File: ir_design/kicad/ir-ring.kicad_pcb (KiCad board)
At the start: 2 copper layers, 40.3 x 43.1 mm, 24 parts, among them J1 PicoBlade/MX1.25 5p R/A THT, Q1 AO3400A, U1 SY7200A, U2 TEMT6200FX01

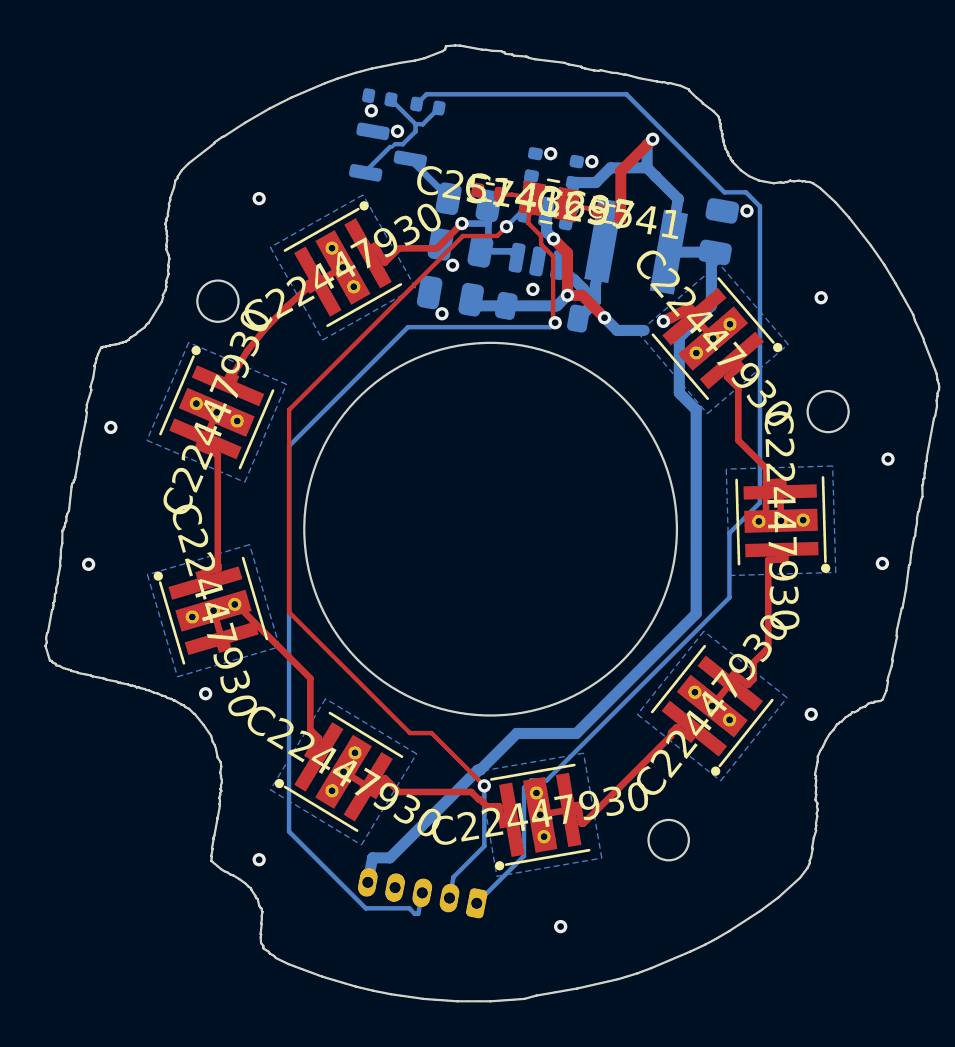
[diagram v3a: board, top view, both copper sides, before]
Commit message: feat(ir): spread the back side, 0805 passives, test pads
Only the switching loop stays packed in the top gap, now with >= 0.3 mm
courtyard gaps (was 0.03-0.1 mm, with L1/C1/C2 cutting into the thermal
islands). The DC-only half-power switch (Q1, R3, R4) moves to the D7-D8 gap;
09 asserts island, screw-head and courtyard clearances.

- all 0402 passives -> 0805; C2 -> 1206 X7R (C29823) for DC-bias margin
- TP1 VOUT (on D2's VOUT island), TP2 FB, TP3 GND, out of the BOM
- power stage pre-routed and closed on B.Cu; Freerouting re-solved it
  differently every run and stopped finding the VOUT crossing
- LCSC field hidden: it was printed on the silkscreen (78 -> 9 silk warnings)

DRC with --schematic-parity: 0 violations, 0 unconnected, 0 footprint errors.

Co-Authored-By: Claude Opus 5.5 <noreply@anthropic.com>
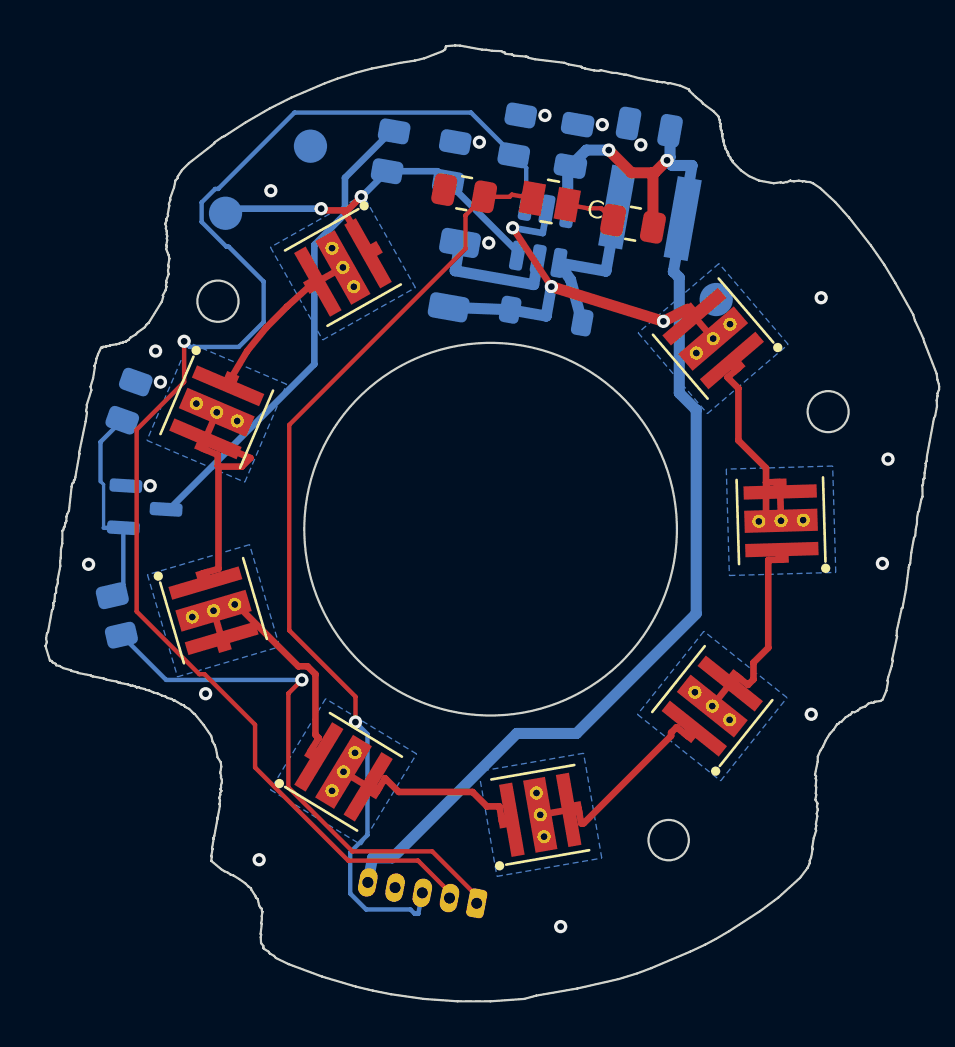
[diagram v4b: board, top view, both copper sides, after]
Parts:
- added TP1: VOUT, TestPoint:TestPoint_Pad_D1.5mm, B.Cu at (158.7, 94.6)
- added TP2: FB, TestPoint:TestPoint_Pad_D1.5mm, B.Cu at (136.5, 90.8)
- added TP3: GND, TestPoint:TestPoint_Pad_D1.5mm, B.Cu at (140.4, 87.7)
- C2: value 4.7uF 50V -> 4.7uF 50V X7R; footprint Capacitor_SMD:C_0805_2012Metric -> Capacitor_SMD:C_1206_3216Metric
- C3: footprint Capacitor_SMD:C_0402_1005Metric -> Capacitor_SMD:C_0805_2012Metric
- R2, R3, R4, R6, R7: footprint Resistor_SMD:R_0402_1005Metric -> Resistor_SMD:R_0805_2012Metric
- moved R3 26.9 mm to (131.6, 108.9), turned to 103 degrees
- moved Q1 19.3 mm to (132.9, 104.0), turned to -3.5 degrees
- moved R4 17.8 mm to (132.2, 99.2), turned to 70.5 degrees
- moved C1 5.66 mm to (155.7, 86.9), turned to 170 degrees
- moved R1b 4.20 mm to (144.0, 88.0), turned to 80 degrees
- moved R1a 3.89 mm to (146.7, 88.4), turned to 80 degrees
- moved L1 1.64 mm to (155.7, 90.7)
- moved R2 1.51 mm to (149.7, 87.2)
- moved C3 1.21 mm to (152.3, 87.7)
- moved R7 1.14 mm to (154.9, 91.2)
- moved R6 1.11 mm to (147.3, 89.8)
- moved C2 0.96 mm to (146.9, 93.5), turned to 80 degrees
- moved D1 0.24 mm to (151.0, 95.4)
- moved U1 0.10 mm to (150.8, 91.7)
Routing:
- net /WL_EN: track 54.9 -> 24.9 mm, vias 0 -> 1
- net /IL_EN: track 42.8 -> 63.7 mm, vias 2 -> 1
- net /R1B_Q: track 2.49 -> 21.5 mm
- net /FB: track 10.5 -> 18.4 mm, vias 1 -> 2
- net GND: track 0.00 -> 6.04 mm, vias 18 -> 17
- net /LDR: track 47.6 -> 43.5 mm
- net /VOUT: track 15.5 -> 19.2 mm, vias 4 -> 3
- net /Q1_G: track 6.32 -> 9.48 mm
- net /STR6: track 9.44 -> 12.3 mm
- net /SW: track 6.42 -> 8.01 mm
- net +5V: track 54.6 -> 53.6 mm, vias 1 -> 2
- net /U2_C: track 1.50 -> 2.30 mm

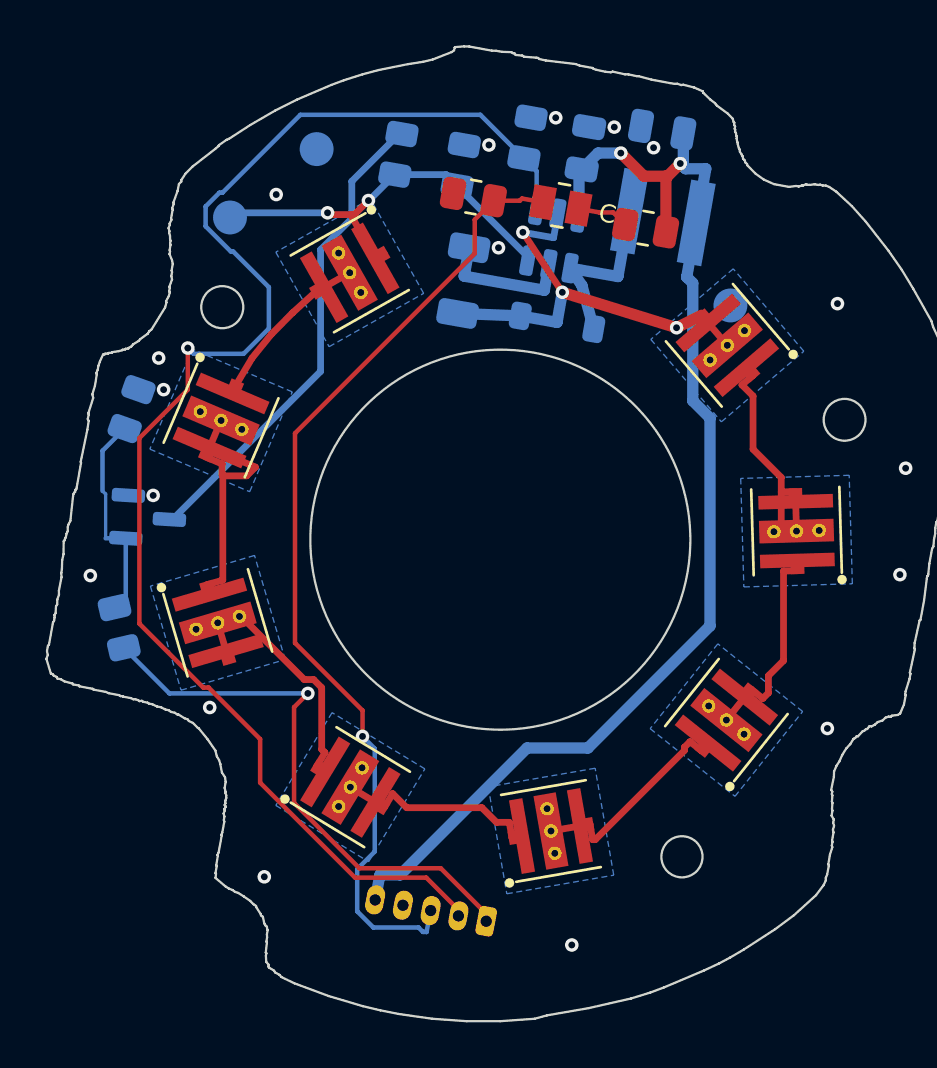
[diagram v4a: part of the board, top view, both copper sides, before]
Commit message: feat(ir): JLCPCB two-layer FR4 fab package
11_fab.py builds ir_design/fab/ from the routed board, and refuses to run
unless DRC with schematic parity is clean: gerbers + drill zip, a grouped
JLCPCB BOM, the CPL (both sides, 12 parts on the back), and cross-checks
(drill hits = vias + plated pads, every BOM line has a placement).

The 2 oz order the plan asks for was not legal as drawn:
- board rules raised to JLCPCB's 2 oz floor, 0.16/0.16 mm, re-routed
- PTH ring >= 0.254 mm enforced in ir-ring.kicad_dru; the stock PicoBlade
  footprint left 0.15 mm (under even the 1 oz floor), so J1 gets 1.05 mm
  pads for a 0.275 mm ring
- the VOUT via moved 0.1 mm off U1's LX pad (was 0.150 mm)

J1 is hand-soldered (no LCSC listing found). ORDER.md lists the options
and the placement-preview checks for the custom footprints.

Co-Authored-By: Claude Opus 5.5 <noreply@anthropic.com>
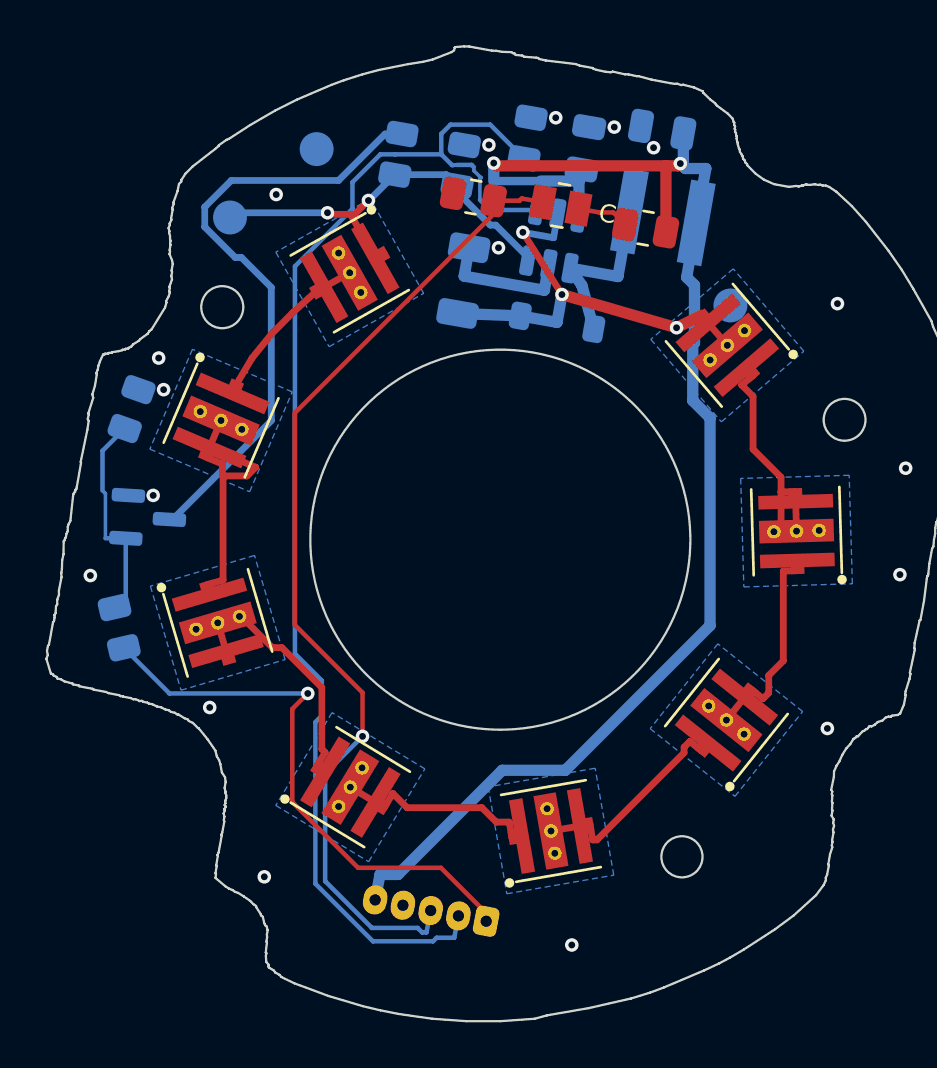
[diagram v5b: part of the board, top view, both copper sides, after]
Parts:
- J1: footprint Connector_Molex:Molex_PicoBlade_53048-0510_1x05_P1.25mm_Horizontal -> ir-ring:Molex_PicoBlade_53048-0510_1x05_P1.25mm_Horizontal_Ring0.275
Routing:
- net +5V: track 53.6 -> 61.7 mm
- net /IL_EN: track 63.7 -> 56.7 mm, vias 1 -> 0
- net /R1B_Q: track 21.5 -> 27.2 mm
- net /LDR: track 43.5 -> 44.3 mm

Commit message: feat(ir): D1 -> B5819W SL (C8598), a JLCPCB Basic part
Same SOD-123 footprint, 40 V 1 A, meets the design's >= 40 V rule over the
33 V open-LED clamp (headroom 27 V -> 7 V). Drops one Extended setup fee;
BOM is now 8 Basic / 6 Extended lines. L1 has no Basic equivalent (Basic
inductors are mA-rated multilayer parts), nor do U1, U2, D2-D9, J1.

Co-Authored-By: Claude Opus 5.5 <noreply@anthropic.com>
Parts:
- D1: value >=40V 1A -> B5819W 40V 1A

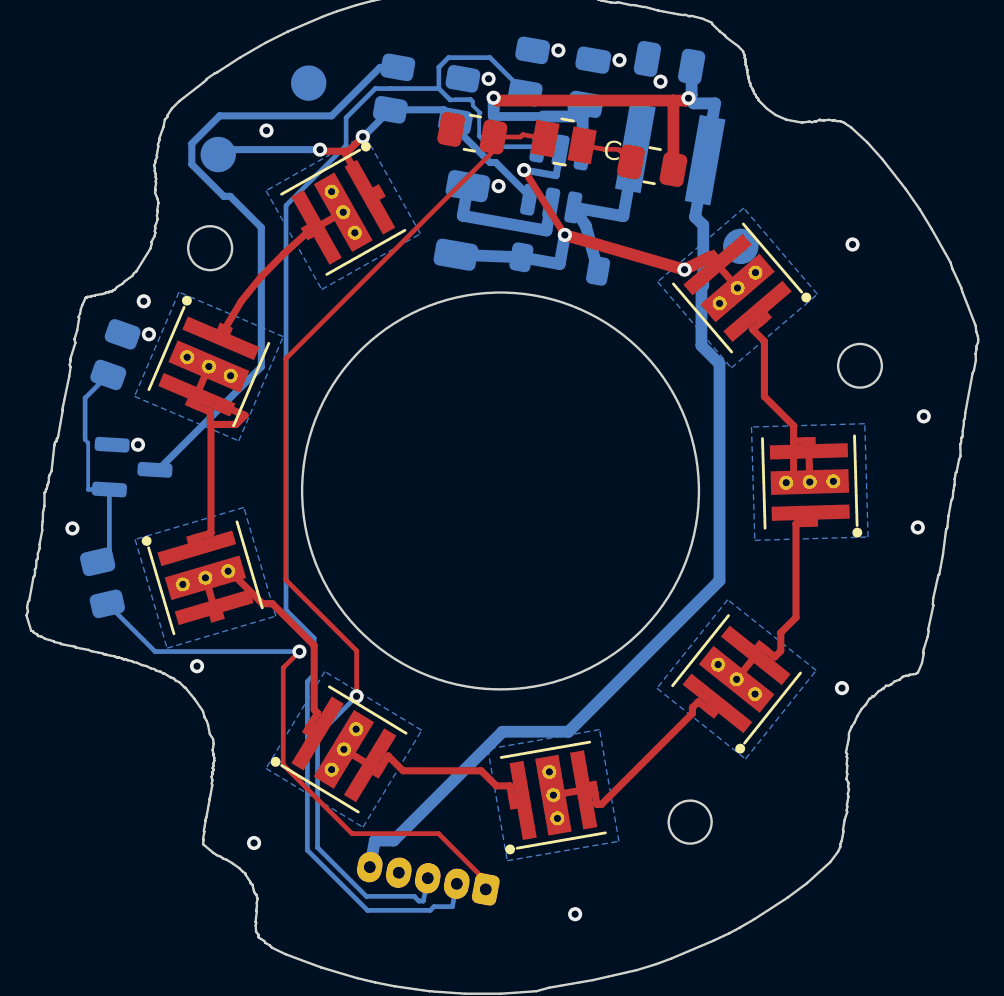
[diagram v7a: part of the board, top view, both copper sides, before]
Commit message: fix(ir): emitter cathode back on the left, matching JLCPCB's library
a2da7caa mirrored the 3535 footprint to put the cathode on the right, reading
the datasheet's pad view as a bottom view. Two sources say otherwise: the
datasheet's own top view (pin 1 left, chamfer at the anode corner) and
JLCPCB's library part for C22447930 (K left, A right). JLCPCB places from its
footprint at our CPL rotation, so the disagreement would have set every
emitter the wrong way round.

That is a short, not a reversed diode: the centre pad is the anode. Eight
shorted emitters put the 5 V rail through L1 and D1 into R1a, even with the
converter off: ~1.1 A, ~5 W in an 0805, and FB at ~4.8 V against a 4 V
absolute maximum.

No copper moved. 09_place.py orients each emitter by its anode->cathode pad
vector, so every emitter turned 180 degrees and its pads landed where they
were: all pads, nets and 245 tracks are identical before and after. The
ir-ring.ses placements for D2-D9 turn by the same 180, because KiCad's SES
import applies them. DRC with schematic parity is clean.

ORDER.md: the U2 check was a trap. JLCPCB numbers the TEMT6200's emitter as
pin 1, so its dot correctly sits away from our "C"; the old note would have
had it rotated backwards.

Co-Authored-By: Claude Opus 5.5 <noreply@anthropic.com>
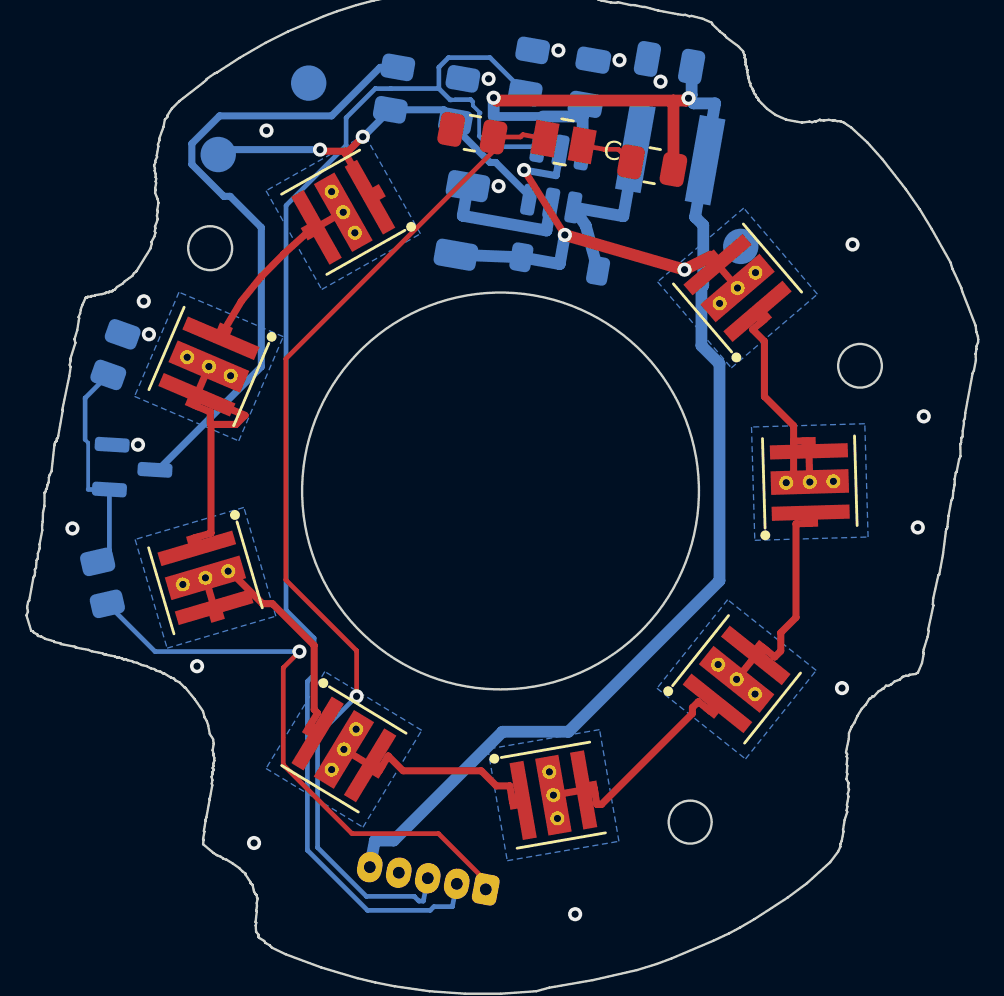
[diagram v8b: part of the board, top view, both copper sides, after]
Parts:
- turned D2 to 130.57 degrees
- turned D3 to 91.66 degrees
- turned D4 to 51.41 degrees
- turned D5 to 9.86 degrees
- turned D6 to -31.22 degrees
- turned D7 to -73.6 degrees
- turned D8 to -113.11 degrees
- turned D9 to -150.57 degrees
